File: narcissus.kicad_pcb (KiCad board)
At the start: 2 copper layers, 115 x 148 mm, 71 parts, among them J1 NEIGHBOR1, J2 NEIGHBOR2, U1 PCA9698, U2 PCA9698, U3 AP2553W6-7, U4 74HC4051

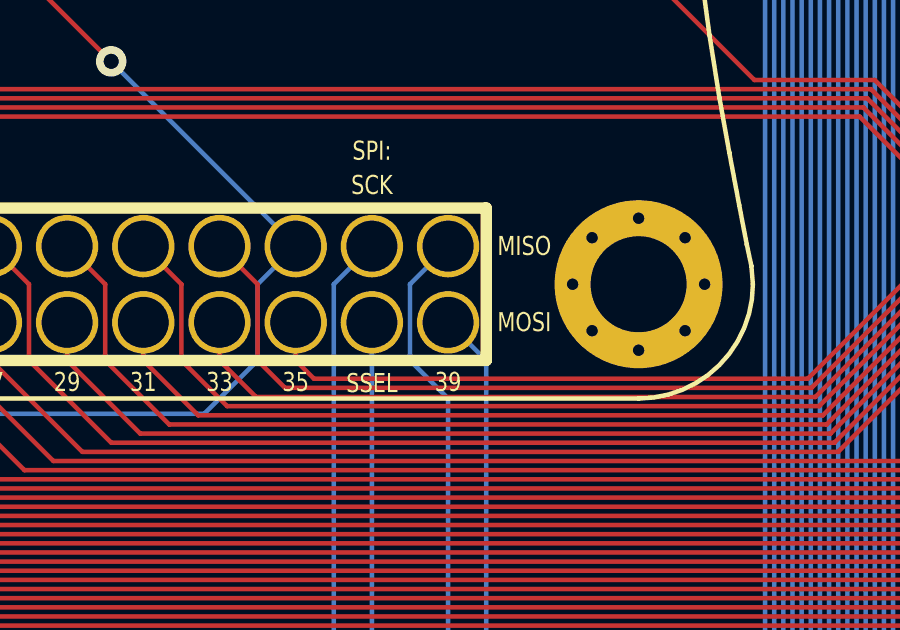
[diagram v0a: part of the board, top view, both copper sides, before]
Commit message: adopt OSHWA convention for SPI signal names https://www.oshwa.org/a-resolution-to-redefine-spi-signal-names
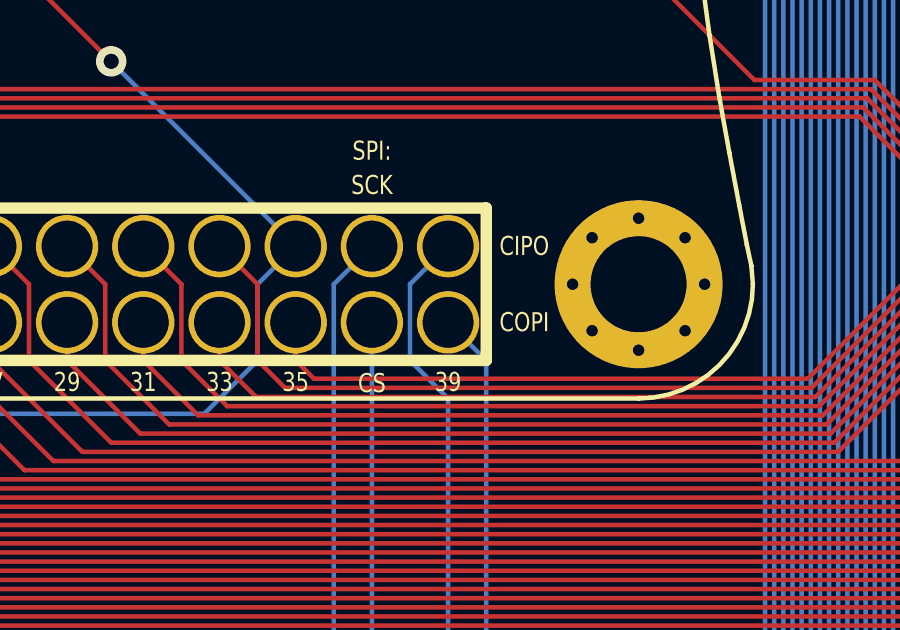
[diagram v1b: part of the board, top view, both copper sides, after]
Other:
- board text added: "CIPO"
- board text added: "COPI"
- board text added: "CS"
- board text removed: "MISO"
- board text removed: "MOSI"
- board text removed: "SSEL"
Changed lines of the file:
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@@
     (effects (font (size 0.635 0.508) (thickness 0.1016)))
   )
-  (gr_text SSEL (at 199.39 116.332) (layer F.SilkS)
+  (gr_text CS (at 199.39 116.332) (layer F.SilkS)
     (effects (font (size 0.635 0.508) (thickness 0.1016)))
   )
-  (gr_text MISO (at 204.47 111.76) (layer F.SilkS)
+  (gr_text CIPO (at 204.47 111.76) (layer F.SilkS)
     (effects (font (size 0.635 0.508) (thickness 0.1016)))
   )
-  (gr_text MOSI (at 204.47 114.3) (layer F.SilkS)
+  (gr_text COPI (at 204.47 114.3) (layer F.SilkS)
     (effects (font (size 0.635 0.508) (thickness 0.1016)))
   )
